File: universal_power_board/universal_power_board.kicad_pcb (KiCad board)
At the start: 2 copper layers, 77 x 75 mm, 100 parts, among them J1 Pixhawk Power, J10 5V OUTPUT, J11 BATT OUTPUT, J12 BATT OUTPUT, J2 BATT INPUT, J3 BATT OUTPUT, J4 5V OUTPUT, J5 5V OUTPUT, J6 BATT OUTPUT, J7 5V OUTPUT, J8 5V OUTPUT, J9 5V OUTPUT, U1 OKL-T_6-W12N-C

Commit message: update v1.1
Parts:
- removed the C1 at (160.5, 132.4)
- removed the C1 at (122.0, 132.4)
- removed the C1 at (160.5, 94.9)
- removed the C1 at (122.0, 94.9)
- removed the J10 at (184.5, 140.0)
- removed the J10 at (146.0, 140.0)
- removed the J10 at (184.5, 102.5)
- removed the J10 at (146.0, 102.5)
- removed the J11 at (173.0, 119.5)
- removed the J11 at (134.5, 119.5)
- removed the J11 at (173.0, 82.0)
- removed the J12 at (179.5, 119.5)
- removed the J12 at (141.0, 119.5)
- removed the J12 at (179.5, 82.0)
- removed the J3 at (166.5, 119.5)
- removed the J3 at (128.0, 119.5)
- removed the J3 at (166.5, 82.0)
- removed the J4 at (184.5, 129.0)
- removed the J4 at (146.0, 129.0)
- removed the J4 at (184.5, 91.5)
- removed the J4 at (146.0, 91.5)
- removed the J5 at (184.5, 134.5)
- removed the J5 at (146.0, 134.5)
- removed the J5 at (184.5, 97.0)
- removed the J5 at (146.0, 97.0)
- removed the J6 at (160.0, 119.5)
- removed the J6 at (121.5, 119.5)
- removed the J6 at (160.0, 82.0)
- removed the J7 at (172.5, 146.5)
- removed the J7 at (134.0, 146.5)
- removed the J7 at (172.5, 109.0)
- removed the J7 at (134.0, 109.0)
- removed the J8 at (178.0, 146.5)
- removed the J8 at (139.5, 146.5)
- removed the J8 at (178.0, 109.0)
- removed the J8 at (139.5, 109.0)
- removed the J9 at (184.5, 123.5)
- removed the J9 at (146.0, 123.5)
- removed the J9 at (184.5, 86.0)
- removed the J9 at (146.0, 86.0)
- added C1: 22uF 25V, Inductor_SMD:L_0805_2012Metric_Pad1.15x1.40mm_HandSolder, F.Cu at (160.4, 132.4)
- added C1: 22uF 25V, Inductor_SMD:L_0805_2012Metric_Pad1.15x1.40mm_HandSolder, F.Cu at (121.9, 132.4)
- added C1: 22uF 25V, Inductor_SMD:L_0805_2012Metric_Pad1.15x1.40mm_HandSolder, F.Cu at (160.4, 94.9)
- added C1: 22uF 25V, Inductor_SMD:L_0805_2012Metric_Pad1.15x1.40mm_HandSolder, F.Cu at (121.9, 94.9)
- added J10: 5V OUTPUT, Connector_JST:JST_PH_B2B-PH-K_1x02_P2.00mm_Vertical, F.Cu at (178.7, 144.2)
- added J10: 5V OUTPUT, Connector_JST:JST_PH_B2B-PH-K_1x02_P2.00mm_Vertical, F.Cu at (140.2, 144.2)
- added J10: 5V OUTPUT, Connector_JST:JST_PH_B2B-PH-K_1x02_P2.00mm_Vertical, F.Cu at (178.7, 106.7)
- added J10: 5V OUTPUT, Connector_JST:JST_PH_B2B-PH-K_1x02_P2.00mm_Vertical, F.Cu at (140.2, 106.7)
- added J11: BATT OUTPUT, Connector_AMASS:AMASS_XT30U-F_1x02_P5.0mm_Vertical, F.Cu at (172.5, 114.6)
- added J11: BATT OUTPUT, Connector_AMASS:AMASS_XT30U-F_1x02_P5.0mm_Vertical, F.Cu at (134.0, 114.6)
- added J11: BATT OUTPUT, Connector_AMASS:AMASS_XT30U-F_1x02_P5.0mm_Vertical, F.Cu at (172.5, 77.1)
- added J12: BATT OUTPUT, Connector_AMASS:AMASS_XT30U-F_1x02_P5.0mm_Vertical, F.Cu at (178.7, 114.6)
- added J12: BATT OUTPUT, Connector_AMASS:AMASS_XT30U-F_1x02_P5.0mm_Vertical, F.Cu at (140.2, 114.6)
- added J12: BATT OUTPUT, Connector_AMASS:AMASS_XT30U-F_1x02_P5.0mm_Vertical, F.Cu at (178.7, 77.1)
- added J3: BATT OUTPUT, Connector_AMASS:AMASS_XT30U-F_1x02_P5.0mm_Vertical, F.Cu at (166.3, 114.6)
- added J3: BATT OUTPUT, Connector_AMASS:AMASS_XT30U-F_1x02_P5.0mm_Vertical, F.Cu at (127.8, 114.6)
- added J3: BATT OUTPUT, Connector_AMASS:AMASS_XT30U-F_1x02_P5.0mm_Vertical, F.Cu at (166.3, 77.1)
- added J4: 5V OUTPUT, Connector_JST:JST_PH_B2B-PH-K_1x02_P2.00mm_Vertical, F.Cu at (184.3, 122.3)
- added J4: 5V OUTPUT, Connector_JST:JST_PH_B2B-PH-K_1x02_P2.00mm_Vertical, F.Cu at (145.8, 122.3)
- added J4: 5V OUTPUT, Connector_JST:JST_PH_B2B-PH-K_1x02_P2.00mm_Vertical, F.Cu at (184.3, 84.8)
- added J4: 5V OUTPUT, Connector_JST:JST_PH_B2B-PH-K_1x02_P2.00mm_Vertical, F.Cu at (145.8, 84.8)
- added J5: 5V OUTPUT, Connector_JST:JST_PH_B2B-PH-K_1x02_P2.00mm_Vertical, F.Cu at (184.3, 127.9)
- added J5: 5V OUTPUT, Connector_JST:JST_PH_B2B-PH-K_1x02_P2.00mm_Vertical, F.Cu at (145.8, 127.9)
- added J5: 5V OUTPUT, Connector_JST:JST_PH_B2B-PH-K_1x02_P2.00mm_Vertical, F.Cu at (184.3, 90.4)
- added J5: 5V OUTPUT, Connector_JST:JST_PH_B2B-PH-K_1x02_P2.00mm_Vertical, F.Cu at (145.8, 90.4)
- added J6: BATT OUTPUT, Connector_AMASS:AMASS_XT30U-F_1x02_P5.0mm_Vertical, F.Cu at (160.1, 114.6)
- added J6: BATT OUTPUT, Connector_AMASS:AMASS_XT30U-F_1x02_P5.0mm_Vertical, F.Cu at (121.6, 114.6)
- added J6: BATT OUTPUT, Connector_AMASS:AMASS_XT30U-F_1x02_P5.0mm_Vertical, F.Cu at (160.1, 77.1)
- added J7: 5V OUTPUT, Connector_JST:JST_PH_B2B-PH-K_1x02_P2.00mm_Vertical, F.Cu at (184.3, 133.5)
- added J7: 5V OUTPUT, Connector_JST:JST_PH_B2B-PH-K_1x02_P2.00mm_Vertical, F.Cu at (145.8, 133.5)
- added J7: 5V OUTPUT, Connector_JST:JST_PH_B2B-PH-K_1x02_P2.00mm_Vertical, F.Cu at (184.3, 96.0)
- added J7: 5V OUTPUT, Connector_JST:JST_PH_B2B-PH-K_1x02_P2.00mm_Vertical, F.Cu at (145.8, 96.0)
- added J8: 5V OUTPUT, Connector_JST:JST_PH_B2B-PH-K_1x02_P2.00mm_Vertical, F.Cu at (184.3, 139.1)
- added J8: 5V OUTPUT, Connector_JST:JST_PH_B2B-PH-K_1x02_P2.00mm_Vertical, F.Cu at (145.8, 139.1)
- added J8: 5V OUTPUT, Connector_JST:JST_PH_B2B-PH-K_1x02_P2.00mm_Vertical, F.Cu at (184.3, 101.6)
- added J8: 5V OUTPUT, Connector_JST:JST_PH_B2B-PH-K_1x02_P2.00mm_Vertical, F.Cu at (145.8, 101.6)
- added J9: 5V OUTPUT, Connector_JST:JST_PH_B2B-PH-K_1x02_P2.00mm_Vertical, F.Cu at (173.1, 144.2)
- added J9: 5V OUTPUT, Connector_JST:JST_PH_B2B-PH-K_1x02_P2.00mm_Vertical, F.Cu at (134.6, 144.2)
- added J9: 5V OUTPUT, Connector_JST:JST_PH_B2B-PH-K_1x02_P2.00mm_Vertical, F.Cu at (173.1, 106.7)
- added J9: 5V OUTPUT, Connector_JST:JST_PH_B2B-PH-K_1x02_P2.00mm_Vertical, F.Cu at (134.6, 106.7)
- added REF1: Fiducial_1mm_Mask2mm, Fiducial:Fiducial_1mm_Mask2mm, F.Cu at (127.0, 69.1)
- added REF2: Fiducial_1mm_Mask2mm, Fiducial:Fiducial_1mm_Mask2mm, F.Cu at (174.0, 154.1)
- J2 (x4): value BATT INPUT -> BATT INPUT MAX14V
- moved J12 4.96 mm to (140.2, 77.1), turned to 270 degrees
- moved J11 4.93 mm to (134.0, 77.1), turned to 270 degrees
- moved J3 4.90 mm to (127.8, 77.1), turned to 270 degrees
- moved J6 4.90 mm to (121.6, 77.1), turned to 270 degrees
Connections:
- J11 pad 1: +BATT -> GND
- J11 pad 2: GND -> +BATT
- J12 pad 1: +BATT -> GND
- J12 pad 2: GND -> +BATT
- J3 pad 1: +BATT -> GND
- J3 pad 2: GND -> +BATT
- J6 pad 1: +BATT -> GND
- J6 pad 2: GND -> +BATT
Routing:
- net +5V: track 268.8 -> 813.1 mm, vias 0 -> 100
- net GND: track 527.2 -> 43.9 mm, vias 0 -> 208
- net +BATT: track 206.8 -> 639.8 mm, vias 0 -> 64
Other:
- board size 77 x 75 mm -> 77 x 95 mm
- board text added: "UNIVERSAL POWER BOARD V1.1"
- board text removed: "UNIVERSAL POWER BOARD V1.0"

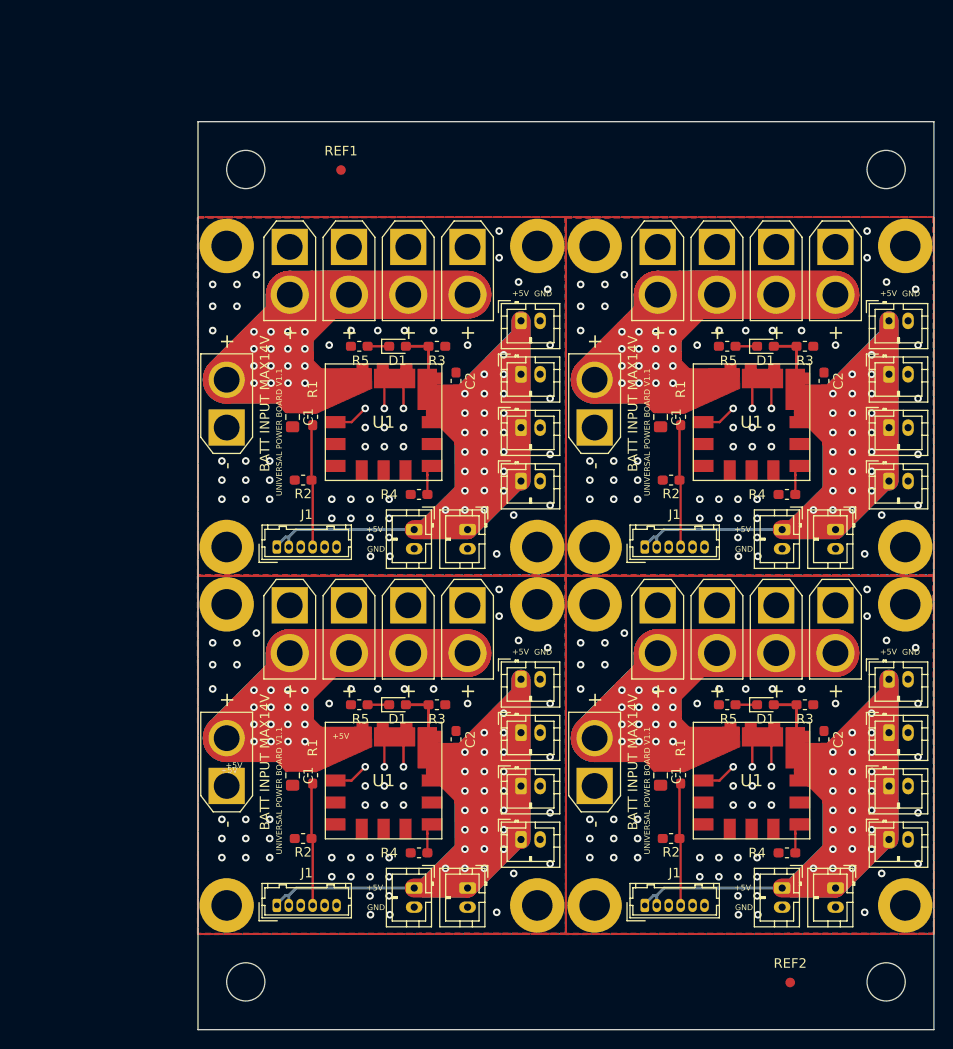
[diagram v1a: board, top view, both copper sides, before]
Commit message: kicad6対応
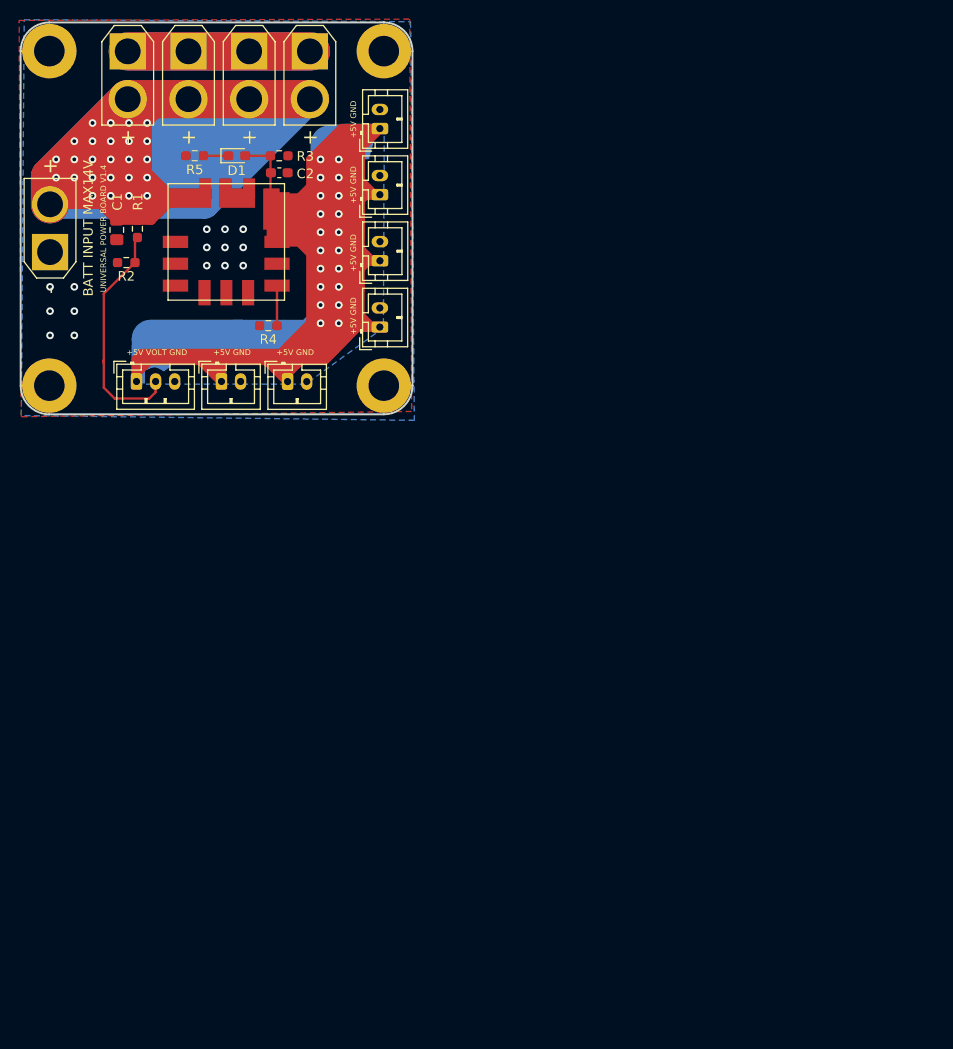
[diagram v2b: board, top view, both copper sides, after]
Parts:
- removed the C1 at (160.4, 132.4)
- removed the C1 at (121.9, 132.4)
- removed the C1 at (160.4, 94.9)
- removed the C1 at (121.9, 94.9)
- removed the C2 at (177.5, 128.6)
- removed the C2 at (139.0, 128.6)
- removed the C2 at (177.5, 91.1)
- removed the C2 at (139.0, 91.1)
- removed the D1 at (171.4, 125.0)
- removed the D1 at (132.9, 125.0)
- removed the D1 at (171.4, 87.5)
- removed the D1 at (132.9, 87.5)
- removed the H1 at (153.5, 114.5)
- removed the H1 at (115.0, 114.5)
- removed the H1 at (153.5, 77.0)
- removed the H1 at (115.0, 77.0)
- removed the H2 at (153.5, 146.0)
- removed the H2 at (115.0, 146.0)
- removed the H2 at (153.5, 108.5)
- removed the H2 at (115.0, 108.5)
- removed the H3 at (186.0, 114.5)
- removed the H3 at (147.5, 114.5)
- removed the H3 at (186.0, 77.0)
- removed the H3 at (147.5, 77.0)
- removed the H4 at (186.0, 146.0)
- removed the H4 at (147.5, 146.0)
- removed the H4 at (186.0, 108.5)
- removed the H4 at (147.5, 108.5)
- removed the J1 at (158.8, 146.0)
- removed the J1 at (120.2, 146.0)
- removed the J1 at (158.8, 108.5)
- removed the J1 at (120.2, 108.5)
- removed the J10 at (178.7, 144.2)
- removed the J10 at (140.2, 144.2)
- removed the J10 at (178.7, 106.7)
- removed the J10 at (140.2, 106.7)
- removed the J11 at (172.5, 114.6)
- removed the J11 at (134.0, 114.6)
- removed the J11 at (172.5, 77.1)
- removed the J11 at (134.0, 77.1)
- removed the J12 at (178.7, 114.6)
- removed the J12 at (140.2, 114.6)
- removed the J12 at (178.7, 77.1)
- removed the J12 at (140.2, 77.1)
- removed the J2 at (153.5, 133.5)
- removed the J2 at (115.0, 133.5)
- removed the J2 at (153.5, 96.0)
- removed the J2 at (115.0, 96.0)
- removed the J3 at (166.3, 114.6)
- removed the J3 at (127.8, 114.6)
- removed the J3 at (166.3, 77.1)
- removed the J3 at (127.8, 77.1)
- removed the J4 at (184.3, 122.3)
- removed the J4 at (145.8, 122.3)
- removed the J4 at (184.3, 84.8)
- removed the J4 at (145.8, 84.8)
- removed the J5 at (184.3, 127.9)
- removed the J5 at (145.8, 127.9)
- removed the J5 at (184.3, 90.4)
- removed the J5 at (145.8, 90.4)
- removed the J6 at (160.1, 114.6)
- removed the J6 at (121.6, 114.6)
- removed the J6 at (160.1, 77.1)
- removed the J6 at (121.6, 77.1)
- removed the J7 at (184.3, 133.5)
- removed the J7 at (145.8, 133.5)
- removed the J7 at (184.3, 96.0)
- removed the J7 at (145.8, 96.0)
- removed the J8 at (184.3, 139.1)
- removed the J8 at (145.8, 139.1)
- removed the J8 at (184.3, 101.6)
- removed the J8 at (145.8, 101.6)
- removed the J9 at (173.1, 144.2)
- removed the J9 at (134.6, 144.2)
- removed the J9 at (173.1, 106.7)
- removed the J9 at (134.6, 106.7)
- removed the R1 at (162.5, 132.4)
- removed the R1 at (124.0, 132.4)
- removed the R1 at (162.5, 94.9)
- removed the R1 at (124.0, 94.9)
- removed the R2 at (161.5, 139.0)
- removed the R2 at (123.0, 139.0)
- removed the R2 at (161.5, 101.5)
- removed the R2 at (123.0, 101.5)
- removed the R3 at (175.5, 125.0)
- removed the R3 at (137.0, 125.0)
- removed the R3 at (175.5, 87.5)
- removed the R3 at (137.0, 87.5)
- removed the R4 at (173.6, 140.5)
- removed the R4 at (135.1, 140.5)
- removed the R4 at (173.6, 103.0)
- removed the R4 at (135.1, 103.0)
- removed the R5 at (167.4, 125.0)
- removed the R5 at (128.9, 125.0)
- removed the R5 at (167.4, 87.5)
- removed the R5 at (128.9, 87.5)
- removed REF1, REF2: Fiducial_1mm_Mask2mm, Fiducial:Fiducial_1mm_Mask2mm
- removed the U1 at (176.0, 139.0)
- removed the U1 at (137.5, 139.0)
- removed the U1 at (176.0, 101.5)
- removed the U1 at (137.5, 101.5)
- added C1: 22uF 25V, Inductor_SMD:L_0805_2012Metric_Pad1.15x1.40mm_HandSolder, F.Cu at (103.5, 75.3)
- added C2: 10uF 10V, Inductor_SMD:L_0603_1608Metric_Pad1.05x0.95mm_HandSolder, F.Cu at (120.5, 69.3)
- added D1: LED, LED_SMD:LED_0603_1608Metric_Pad1.05x0.95mm_HandSolder, F.Cu at (116.1, 67.6)
- added H1: MountingHole, MountingHole:MountingHole_3.2mm_M3_ISO7380_Pad, F.Cu at (96.4, 91.6)
- added H2: MountingHole, MountingHole:MountingHole_3.2mm_M3_ISO7380_Pad, F.Cu at (131.4, 56.6)
- added H3: MountingHole, MountingHole:MountingHole_3.2mm_M3_ISO7380_Pad, F.Cu at (96.4, 56.6)
- added H4: MountingHole, MountingHole:MountingHole_3.2mm_M3_ISO7380_Pad, F.Cu at (131.4, 91.6)
- added J1: Conn_01x03_Male, Connector_JST:JST_PH_B3B-PH-K_1x03_P2.00mm_Vertical, F.Cu at (105.6, 91.2)
- added J10: 5V OUTPUT, Connector_JST:JST_PH_B2B-PH-K_1x02_P2.00mm_Vertical, F.Cu at (121.4, 91.2)
- added J11: BATT OUTPUT, Connector_AMASS:AMASS_XT30U-F_1x02_P5.0mm_Vertical, F.Cu at (117.4, 56.6)
- added J12: BATT OUTPUT, Connector_AMASS:AMASS_XT30U-F_1x02_P5.0mm_Vertical, F.Cu at (123.7, 56.6)
- added J2: BATT INPUT MAX14V, Connector_AMASS:AMASS_XT30U-M_1x02_P5.0mm_Vertical, F.Cu at (96.5, 77.6)
- added J3: BATT OUTPUT, Connector_AMASS:AMASS_XT30U-F_1x02_P5.0mm_Vertical, F.Cu at (104.6, 56.6)
- added J4: 5V OUTPUT, Connector_JST:JST_PH_B2B-PH-K_1x02_P2.00mm_Vertical, F.Cu at (131.0, 64.7)
- added J5: 5V OUTPUT, Connector_JST:JST_PH_B2B-PH-K_1x02_P2.00mm_Vertical, F.Cu at (131.0, 71.6)
- added J6: BATT OUTPUT, Connector_AMASS:AMASS_XT30U-F_1x02_P5.0mm_Vertical, F.Cu at (111.0, 56.6)
- added J7: 5V OUTPUT, Connector_JST:JST_PH_B2B-PH-K_1x02_P2.00mm_Vertical, F.Cu at (131.0, 78.5)
- added J8: 5V OUTPUT, Connector_JST:JST_PH_B2B-PH-K_1x02_P2.00mm_Vertical, F.Cu at (131.0, 85.5)
- added J9: 5V OUTPUT, Connector_JST:JST_PH_B2B-PH-K_1x02_P2.00mm_Vertical, F.Cu at (114.5, 91.2)
- added R1: 1K, Resistor_SMD:R_0603_1608Metric_Pad0.98x0.95mm_HandSolder, F.Cu at (105.7, 75.2)
- added R2: 150, Resistor_SMD:R_0603_1608Metric_Pad0.98x0.95mm_HandSolder, F.Cu at (104.5, 78.7)
- added R3: 20K, Resistor_SMD:R_0603_1608Metric_Pad0.98x0.95mm_HandSolder, F.Cu at (120.5, 67.6)
- added R4: 1.33K, Resistor_SMD:R_0603_1608Metric_Pad0.98x0.95mm_HandSolder, F.Cu at (119.4, 85.3)
- added R5: 300, Resistor_SMD:R_0603_1608Metric_Pad0.98x0.95mm_HandSolder, F.Cu at (111.7, 67.6)
- added U1: OKL-T_6-W12N-C, OKL-T_6-W12N-C:OKL-T_3-W5, F.Cu at (121.1, 82.7)
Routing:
- net +5V: track 813.1 -> 247.2 mm, vias 100 -> 20
- net +BATT: track 639.8 -> 165.9 mm, vias 64 -> 25
- net Net-(J1-Pad4): track 51.4 -> 0.00 mm
- net Net-(J1-Pad2): track 0.00 -> 24.7 mm
- net Net-(R4-Pad1): track 11.9 -> 4.19 mm
- net Net-(D1-Pad1): track 9.00 -> 2.62 mm
- net GND: track 43.9 -> 38.4 mm, vias 208 -> 15
- added copper zone on B.Cu, net +5V
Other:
- board size 77 x 95 mm -> 41 x 41 mm
- net class 5V removed
- net class BATT removed
- net class Default removed
- rule pad_to_mask_clearance: 0.051 -> 0
- board text added: "+5V GND"
- board text added: "+5V VOLT GND"
- board text added: "UNIVERSAL POWER BOARD V1.4"
- board text removed: "+5V"
- board text removed: "GND"
- board text removed: "UNIVERSAL POWER BOARD V1.1"
- board text removed: "V-CUT"
